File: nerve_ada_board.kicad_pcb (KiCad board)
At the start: 4 copper layers, 100 x 100 mm, 66 parts, among them J1 TC2050-IDC, J10 PC1-3, J11 PB4-5, J12 Camera, J2 472192001, J3 2171750001, J6 WS2812B, J7 CAN1, J8 CAN2, J9 PA4-7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

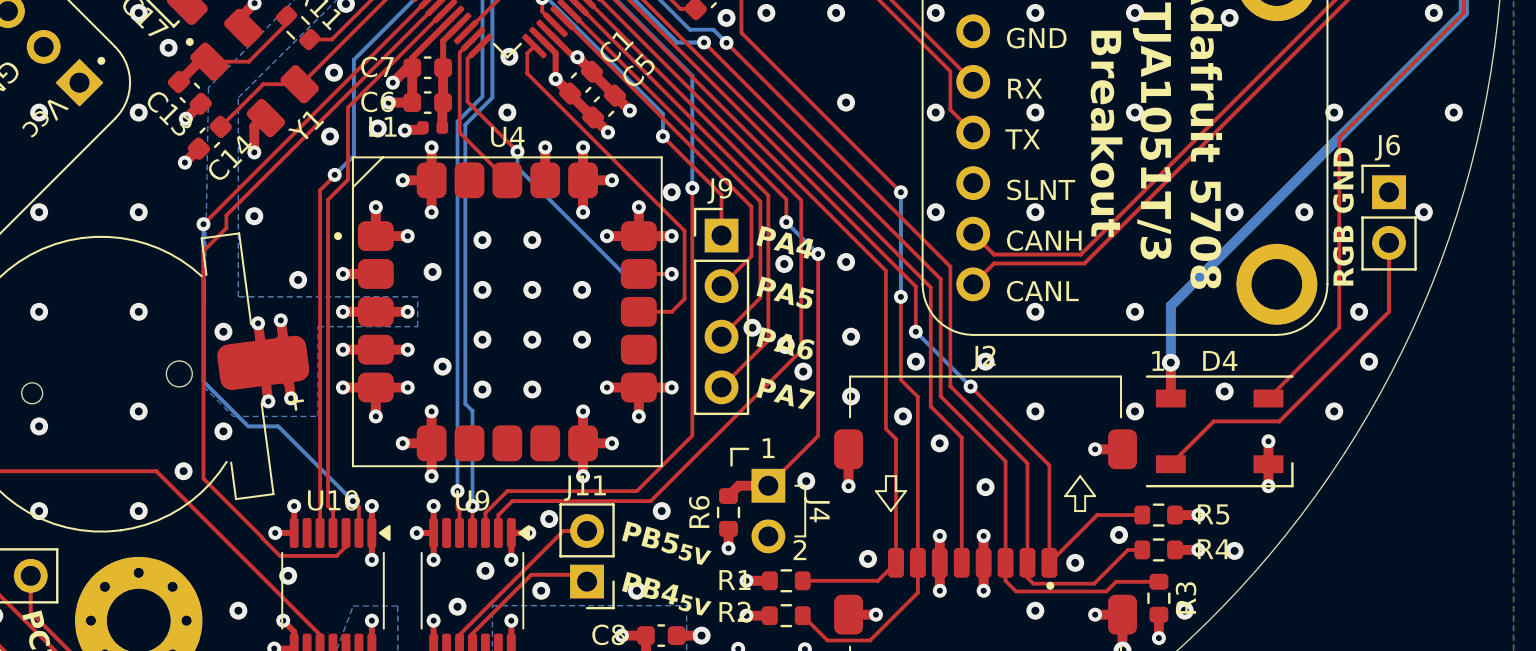
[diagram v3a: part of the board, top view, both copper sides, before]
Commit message: Update J6 WS2812B connector pin order
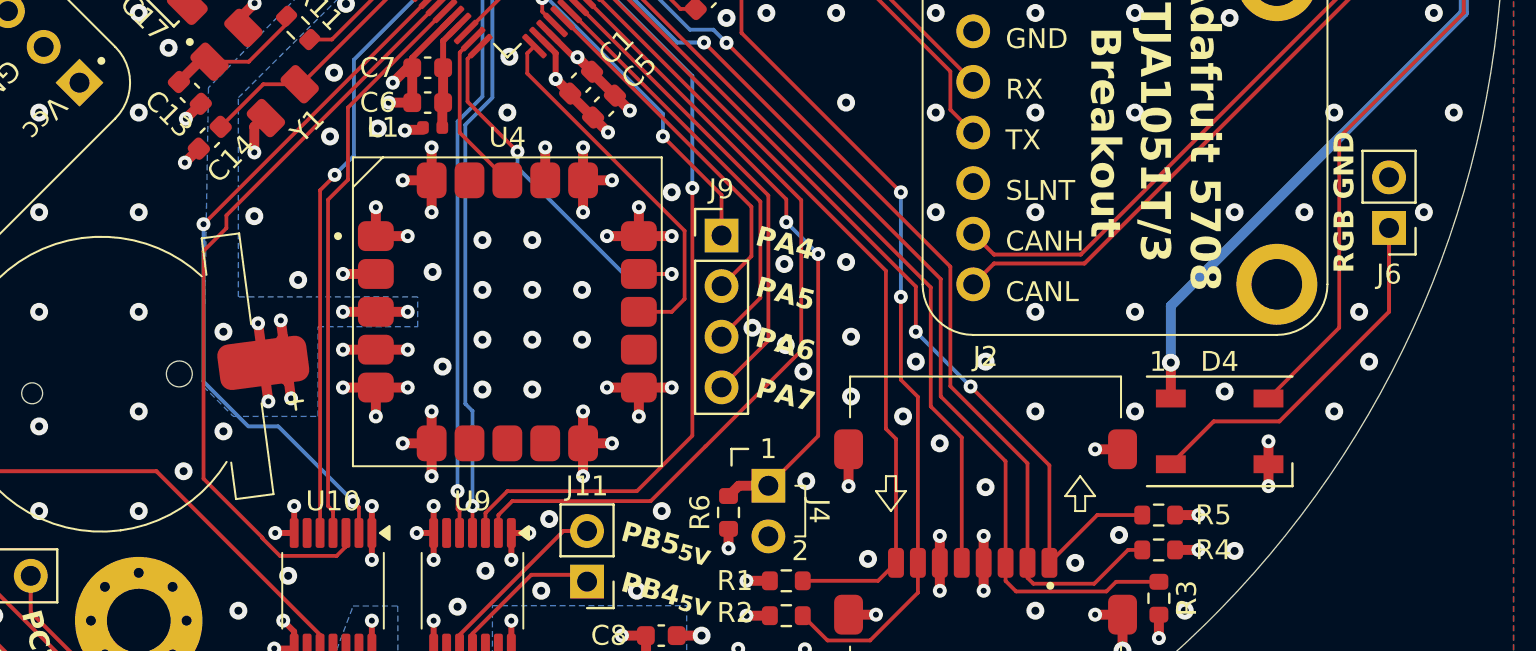
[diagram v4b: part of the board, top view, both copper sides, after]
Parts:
- moved J6 1.79 mm to (192.8, 120.8), turned to 180 degrees
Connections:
- J6 pad 1: GND -> Net-(D4-DOUT)
- J6 pad 2: Net-(D4-DOUT) -> GND
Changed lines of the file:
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@@
 		(tags "capacitor")
 		(property "Reference" "C15"
-			(at 3 0 225)
+			(at 3 0 -135)
 			(layer "F.SilkS")
 			(effects
@@
 		(fp_arc
 			(start -4.68596 5.727284)
-			(mid -6.687148 3.1689)
+			(mid -6.687149 3.1689)
 			(end -7.4 0)
 			(stroke
@@
 		(at 135.815685 113.012742 -45)
 		(property "Reference" "Y1"
-			(at 3.749999 0 225)
+			(at 3.749999 0 -135)
 			(layer "F.SilkS")
 			(effects
@@
 	(footprint "Connector_PinHeader_2.54mm:PinHeader_1x02_P2.54mm_Vertical"
 		(layer "F.Cu")
-		(at 192.75 119)
+		(at 192.75 120.79 180)
 		(descr "Through hole straight pin header, 1x02, 2.54mm pitch, single row")
 		(tags "Through hole pin header THT 1x02 2.54mm single row")
 		(property "Reference" "J6"
-			(at 0 -2.33 0)
+			(at 0 -2.33 360)
 			(layer "F.SilkS")
 			(effects
@@
 		)
 		(property "Value" "WS2812B"
-			(at 0 4.87 0)
+			(at 0 4.87 360)
 			(layer "F.Fab")
 			(effects
@@
 		)
 		(property "Footprint" "Connector_PinHeader_2.54mm:PinHeader_1x02_P2.54mm_Vertical"
-			(at 0 0 0)
+			(at 0 0 180)
 			(unlocked yes)
 			(layer "F.Fab")
@@
 		)
 		(property "Datasheet" ""
-			(at 0 0 0)
+			(at 0 0 180)
 			(unlocked yes)
 			(layer "F.Fab")
@@
 		)
 		(property "Description" "Generic connector, single row, 01x02, script generated"
-			(at 0 0 0)
+			(at 0 0 180)
 			(unlocked yes)
 			(layer "F.Fab")
@@
 		(attr through_hole)
 		(fp_line
-			(start -1.33 -1.33)
-			(end 0 -1.33)
+			(start 1.33 1.27)
+			(end 1.33 3.87)
 			(stroke
 				(width 0.12)
@@
 		)
 		(fp_line
-			(start -1.33 0)
-			(end -1.33 -1.33)
+			(start -1.33 3.87)
+			(end 1.33 3.87)
 			(stroke
 				(width 0.12)
@@
 		(fp_line
 			(start -1.33 1.27)
-			(end -1.33 3.87)
+			(end 1.33 1.27)
 			(stroke
 				(width 0.12)
@@
 		(fp_line
 			(start -1.33 1.27)
-			(end 1.33 1.27)
+			(end -1.33 3.87)
 			(stroke
 				(width 0.12)
@@
 		)
 		(fp_line
-			(start -1.33 3.87)
-			(end 1.33 3.87)
+			(start -1.33 0)
+			(end -1.33 -1.33)
 			(stroke
 				(width 0.12)
@@
 		)
 		(fp_line
-			(start 1.33 1.27)
-			(end 1.33 3.87)
+			(start -1.33 -1.33)
+			(end 0 -1.33)
 			(stroke
 				(width 0.12)
@@
 		)
 		(fp_line
-			(start -1.8 -1.8)
-			(end -1.8 4.35)
+			(start 1.8 4.35)
+			(end 1.8 -1.8)
 			(stroke
 				(width 0.05)
@@
 		)
 		(fp_line
-			(start -1.8 4.35)
-			(end 1.8 4.35)
+			(start 1.8 -1.8)
+			(end -1.8 -1.8)
 			(stroke
 				(width 0.05)
@@
 		)
 		(fp_line
-			(start 1.8 -1.8)
-			(end -1.8 -1.8)
+			(start -1.8 4.35)
+			(end 1.8 4.35)
 			(stroke
 				(width 0.05)
@@
 		)
 		(fp_line
-			(start 1.8 4.35)
-			(end 1.8 -1.8)
+			(start -1.8 -1.8)
+			(end -1.8 4.35)
 			(stroke
 				(width 0.05)
@@
 		)
 		(fp_line
-			(start -1.27 -0.635)
-			(end -0.635 -1.27)
+			(start 1.27 3.81)
+			(end -1.27 3.81)
 			(stroke
 				(width 0.1)
@@
 		)
 		(fp_line
-			(start -1.27 3.81)
-			(end -1.27 -0.635)
+			(start 1.27 -1.27)
+			(end 1.27 3.81)
 			(stroke
 				(width 0.1)
@@
 		)
 		(fp_line
-			(start 1.27 -1.27)
-			(end 1.27 3.81)
+			(start -1.27 3.81)
+			(end -1.27 -0.635)
 			(stroke
 				(width 0.1)
@@
 		)
 		(fp_line
-			(start 1.27 3.81)
-			(end -1.27 3.81)
+			(start -1.27 -0.635)
+			(end -0.635 -1.27)
 			(stroke
 				(width 0.1)
@@
 		)
 		(pad "1" thru_hole rect
-			(at 0 0)
+			(at 0 0 180)
 			(size 1.7 1.7)
 			(drill 1)
 			(layers "*.Cu" "*.Mask")
 			(remove_unused_layers no)
-			(net 1 "GND")
+			(net 16 "Net-(D4-DOUT)")
 			(pinfunction "Pin_1")
 			(pintype "passive")
 		)
 		(pad "2" thru_hole oval
-			(at 0 2.54)
+			(at 0 2.54 180)
 			(size 1.7 1.7)
 			(drill 1)
 			(layers "*.Cu" "*.Mask")
 			(remove_unused_layers no)
-			(net 16 "Net-(D4-DOUT)")
+			(net 1 "GND")
 			(pinfunction "Pin_2")
 			(pintype "passive")
@@
 	)
 	(gr_text "RGB GND"
-		(at 190.5 120.25 90)
+		(at 190.5 119.5 90)
 		(layer "F.SilkS")
 		(effects
@@
 	)
 	(segment
-		(start 187.25 130.5)
-		(end 192.75 125)
+		(start 183.95 130.5)
+		(end 187.25 130.5)
 		(width 0.2)
 		(layer "F.Cu")
@@
 	)
 	(segment
-		(start 183.95 130.5)
-		(end 187.25 130.5)
+		(start 181.8 132.65)
+		(end 183.95 130.5)
 		(width 0.2)
 		(layer "F.Cu")
@@
 	)
 	(segment
-		(start 192.75 121.540001)
-		(end 192.750001 121.54)
+		(start 187.25 130.5)
+		(end 192.75 125)
 		(width 0.2)
 		(layer "F.Cu")
@@
 	)
 	(segment
-		(start 181.8 132.65)
-		(end 183.95 130.5)
+		(start 192.75 121.540001)
+		(end 192.750001 121.54)
 		(width 0.2)
 		(layer "F.Cu")
